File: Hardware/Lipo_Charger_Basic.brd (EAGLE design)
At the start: 29.2 x 10.2 mm, 16 parts, among them U1 MCP73831

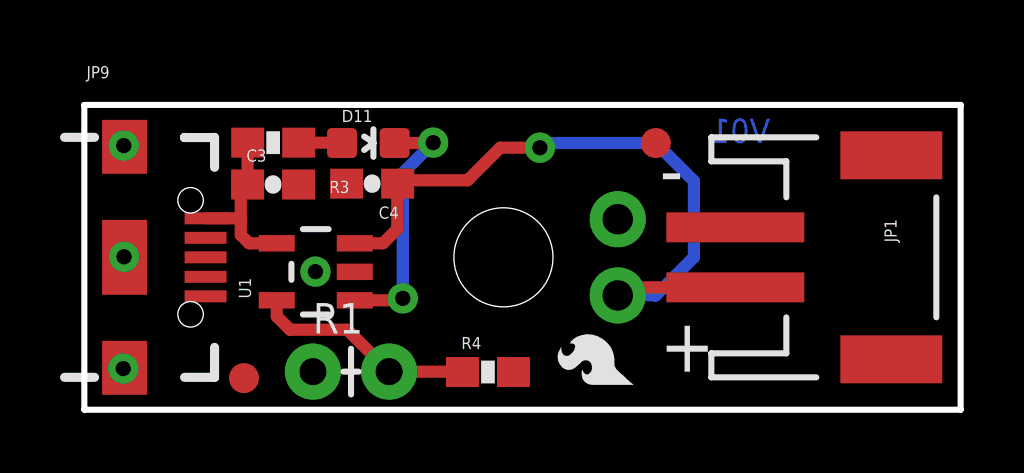
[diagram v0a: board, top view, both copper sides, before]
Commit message: Fixed silk issue, changed rev #'s for reds
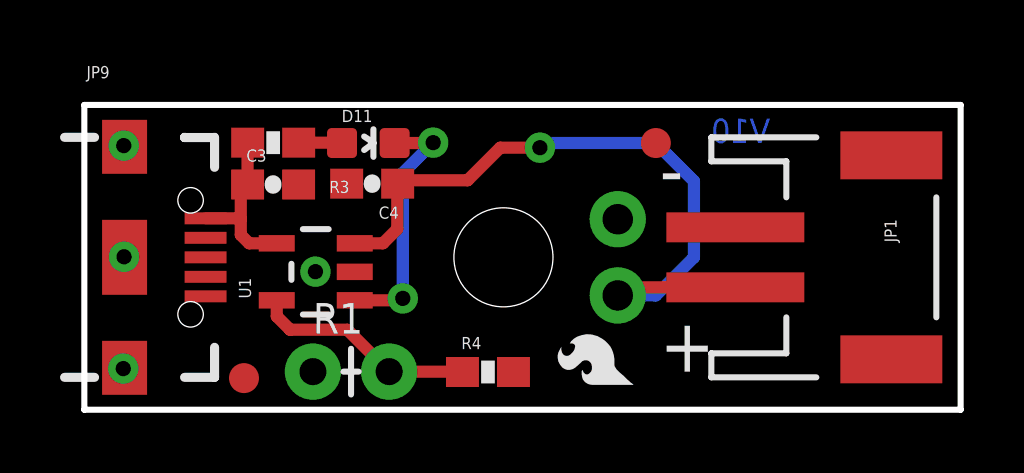
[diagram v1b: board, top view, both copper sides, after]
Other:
- board text added: "V10"
- board text removed: "V01"
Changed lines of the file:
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@@
 <?xml version="1.0" encoding="utf-8"?>
 <!DOCTYPE eagle SYSTEM "eagle.dtd">
-<eagle version="6.4">
+<eagle version="7.2.0">
 <drawing>
 <settings>
@@
 <layer number="56" name="wert" color="7" fill="1" visible="no" active="yes"/>
 <layer number="57" name="tCAD" color="7" fill="1" visible="no" active="no"/>
-<layer number="90" name="Modules" color="5" fill="1" visible="no" active="yes"/>
+<layer number="90" name="Modules" color="5" fill="1" visible="no" active="no"/>
 <layer number="91" name="Nets" color="2" fill="1" visible="no" active="no"/>
 <layer number="92" name="Busses" color="1" fill="1" visible="no" active="no"/>
@@
 <text x="20.955" y="5.461" size="1.778" layer="22" font="vector" ratio="15" rot="MR0">-</text>
 <text x="20.955" y="2.921" size="1.778" layer="22" font="vector" ratio="15" rot="MR0">+</text>
-<text x="23.622" y="0.635" size="1.016" layer="22" font="vector" ratio="15" rot="MR0">LiPo Charger Basic</text>
-<text x="22.86" y="8.89" size="0.8128" layer="16" font="vector" ratio="15" rot="MR0">V01</text>
+<text x="28.321" y="0.635" size="1.016" layer="22" font="vector" ratio="15" rot="MR0">LiPo Charger Basic</text>
+<text x="22.86" y="8.89" size="0.8128" layer="16" font="vector" ratio="15" rot="MR0">V10</text>
 <text x="16.637" y="-11.43" size="1.778" layer="51" font="vector" ratio="10">N. Seidle</text>
 <text x="-1.93548125" y="-14.378940625" size="1.778" layer="51" font="vector" ratio="10">Revised by:Patrick Alberts</text>
@@
 <pass name="Default">
 <param name="RoutingGrid" value="50mil"/>
+<param name="AutoGrid" value="1"/>
+<param name="Efforts" value="0"/>
+<param name="TopRouterVariant" value="1"/>
 <param name="tpViaShape" value="round"/>
 <param name="PrefDir.1" value="|"/>

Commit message: qc cl items fixed
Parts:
- moved C4 0.22 mm to (9.38, 7.51)
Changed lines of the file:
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@@
 <?xml version="1.0" encoding="utf-8"?>
 <!DOCTYPE eagle SYSTEM "eagle.dtd">
-<eagle version="7.2.0">
+<eagle version="6.4">
 <drawing>
 <settings>
@@
 <setting verticaltext="up"/>
 </settings>
-<grid distance="0.05" unitdist="inch" unit="inch" style="lines" multiple="1" display="yes" altdistance="0.005" altunitdist="inch" altunit="inch"/>
+<grid distance="0.05" unitdist="inch" unit="inch" style="lines" multiple="1" display="yes" altdistance="0.0001" altunitdist="inch" altunit="inch"/>
 <layers>
 <layer number="1" name="Top" color="4" fill="1" visible="yes" active="yes"/>
@@
 <layer number="102" name="Vscore" color="7" fill="1" visible="no" active="yes"/>
 <layer number="103" name="tMap" color="7" fill="1" visible="no" active="yes"/>
-<layer number="104" name="Name" color="7" fill="1" visible="no" active="yes"/>
+<layer number="104" name="Name" color="7" fill="1" visible="yes" active="yes"/>
 <layer number="105" name="tPlate" color="7" fill="1" visible="no" active="yes"/>
 <layer number="106" name="bPlate" color="7" fill="1" visible="no" active="yes"/>
@@
 <pass name="Default">
 <param name="RoutingGrid" value="50mil"/>
-<param name="AutoGrid" value="1"/>
-<param name="Efforts" value="0"/>
-<param name="TopRouterVariant" value="1"/>
 <param name="tpViaShape" value="round"/>
 <param name="PrefDir.1" value="|"/>
@@
 </autorouter>
 <elements>
-<element name="D11" library="SparkFun-LED" package="LED-0603" value="RED" x="9.46658125" y="8.89" rot="R270">
+<element name="D11" library="SparkFun-LED" package="LED-0603" value="RED" x="9.46658125" y="8.89" smashed="yes" rot="R270">
 <attribute name="PROD_ID" value="DIO-00819" x="9.46658125" y="8.89" size="1.778" layer="27" rot="R270" display="off"/>
 <attribute name="VALUE" value="RED" x="9.46658125" y="8.89" size="1.778" layer="27" rot="R270" display="off"/>
+<attribute name="NAME" x="8.19658125" y="8.6995" size="0.4064" layer="25"/>
+<attribute name="VALUE" x="9.84758125" y="8.6995" size="0.4064" layer="27"/>
 </element>
 <element name="R3" library="SparkFun-Resistors" package="0603-RES" value="330" x="6.294121875" y="8.9027" smashed="yes" rot="R180">
-<attribute name="NAME" x="8.834121875" y="7.6327" size="0.4064" layer="25" font="vector" rot="R180"/>
 <attribute name="PROD_ID" value="RES-00818" x="6.294121875" y="8.9027" size="1.778" layer="27" rot="R180" display="off"/>
-<attribute name="VALUE" value="330" x="6.294121875" y="8.9027" size="1.778" layer="27" rot="R180" display="off"/>
+<attribute name="NAME" x="7.564121875" y="9.0297" size="0.4064" layer="25" font="vector" rot="R180"/>
+<attribute name="VALUE" x="5.659121875" y="9.0297" size="0.4064" layer="25" font="vector" rot="R180"/>
 </element>
 <element name="U1" library="SparkFun-PowerIC" package="SOT23-5" value="MCP73831" x="7.713984375" y="4.5974" rot="R90">
@@
 </element>
 <element name="JP2" library="SparkFun" package="STAND-OFF" value="STAND-OFF" x="13.97" y="5.08"/>
-<element name="C3" library="SparkFun-Capacitors" package="0603-CAP" value="4.7uF" x="6.29158125" y="7.508240625">
+<element name="C3" library="SparkFun-Capacitors" package="0603-CAP" value="4.7uF" x="6.29158125" y="7.508240625" smashed="yes">
 <attribute name="PROD_ID" value="CAP-08280" x="6.29158125" y="7.508240625" size="1.778" layer="27" display="off"/>
 <attribute name="VALUE" value="4.7uF" x="6.29158125" y="7.508240625" size="1.778" layer="27" display="off"/>
-</element>
-<element name="C4" library="SparkFun-Capacitors" package="0603-CAP" value="4.7uF" x="9.59358125" y="7.536184375" rot="R180">
-<attribute name="PROD_ID" value="CAP-08280" x="9.59358125" y="7.536184375" size="1.778" layer="27" rot="R180" display="off"/>
-<attribute name="VALUE" value="4.7uF" x="9.59358125" y="7.536184375" size="1.778" layer="27" rot="R180" display="off"/>
+<attribute name="NAME" x="5.14858125" y="7.381240625" size="0.4064" layer="25" font="vector"/>
+<attribute name="VALUE" x="6.54558125" y="7.381240625" size="0.4064" layer="27" font="vector"/>
+</element>
+<element name="C4" library="SparkFun-Capacitors" package="0603-CAP" value="4.7uF" x="9.375140625" y="7.505703125" smashed="yes" rot="R180">
+<attribute name="PROD_ID" value="CAP-08280" x="9.375140625" y="7.505703125" size="1.778" layer="27" rot="R180" display="off"/>
+<attribute name="VALUE" value="4.7uF" x="9.375140625" y="7.505703125" size="1.778" layer="27" rot="R180" display="off"/>
+<attribute name="NAME" x="8.994140625" y="7.759703125" size="0.4064" layer="25" font="vector" rot="R180"/>
+<attribute name="VALUE" x="11.661140625" y="7.759703125" size="0.4064" layer="27" font="vector" rot="R180"/>
 </element>
 <element name="JP8" library="SparkFun-Connectors" package="1X02" value="M02PTH" x="17.78" y="6.35" rot="MR270"/>
@@
 <wire x1="15.3416" y1="8.89" x2="19.05" y2="8.89" width="0.4064" layer="16"/>
 <via x="15.186659375" y="8.735059375" extent="1-16" drill="0.508"/>
-<wire x1="10.43178125" y1="6.02488125" x2="10.43178125" y2="7.524384375" width="0.4064" layer="1"/>
-<wire x1="10.43178125" y1="7.524384375" x2="10.44358125" y2="7.536184375" width="0.4064" layer="1"/>
-<wire x1="10.44358125" y1="7.536184375" x2="10.5553375" y2="7.647940625" width="0.4064" layer="1"/>
-<wire x1="10.5553375" y1="7.647940625" x2="12.7762" y2="7.647940625" width="0.4064" layer="1"/>
-<wire x1="12.7762" y1="7.647940625" x2="13.86331875" y2="8.735059375" width="0.4064" layer="1"/>
+<wire x1="12.6339625" y1="7.505703125" x2="13.86331875" y2="8.735059375" width="0.4064" layer="1"/>
 <wire x1="13.86331875" y1="8.735059375" x2="15.186659375" y2="8.735059375" width="0.4064" layer="1"/>
 <wire x1="15.3416" y1="8.89" x2="15.186659375" y2="8.735059375" width="0.4064" layer="16"/>
@@
 <wire x1="9.014084375" y1="5.5474" x2="9.9543" y2="5.5474" width="0.4064" layer="1"/>
 <wire x1="9.9543" y1="5.5474" x2="10.43178125" y2="6.02488125" width="0.4064" layer="1"/>
+<wire x1="10.43178125" y1="6.02488125" x2="10.43178125" y2="7.2990625" width="0.4064" layer="1"/>
+<wire x1="10.43178125" y1="7.2990625" x2="10.225140625" y2="7.505703125" width="0.4064" layer="1"/>
+<wire x1="12.6339625" y1="7.505703125" x2="10.225140625" y2="7.505703125" width="0.4064" layer="1"/>
 </signal>
 <signal name="N$3">
